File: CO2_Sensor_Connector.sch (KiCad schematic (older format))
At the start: 8 parts, among them J1 Conn_01x07_Female, J2 Conn_01x04_Female, Q1 AO3400A, Q2 AO3401A

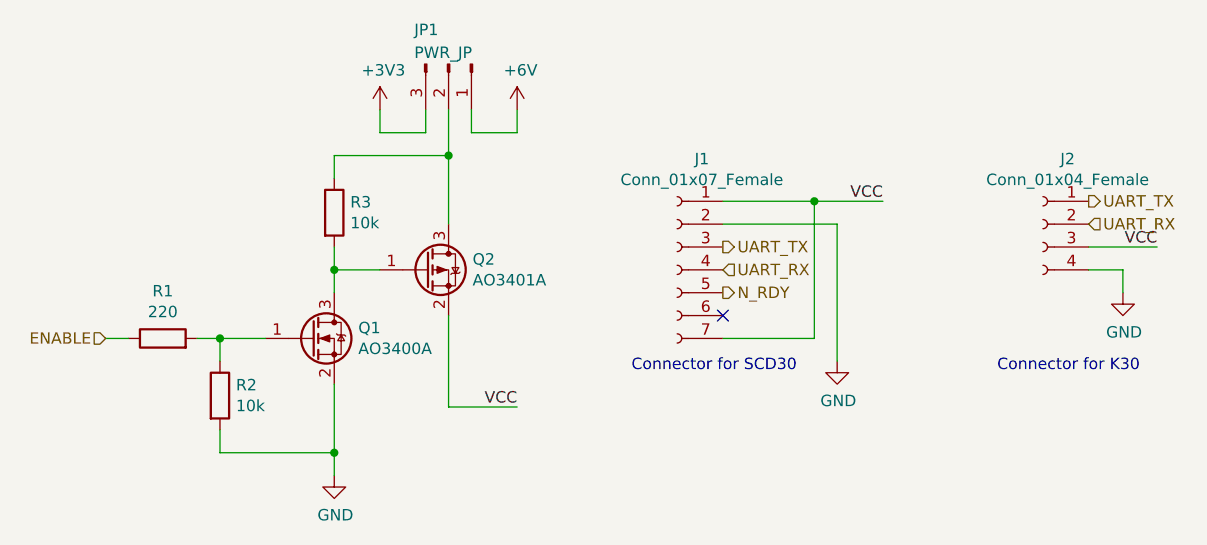
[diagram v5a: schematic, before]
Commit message: Fix sensor PMOS issue and start change to long term chamber
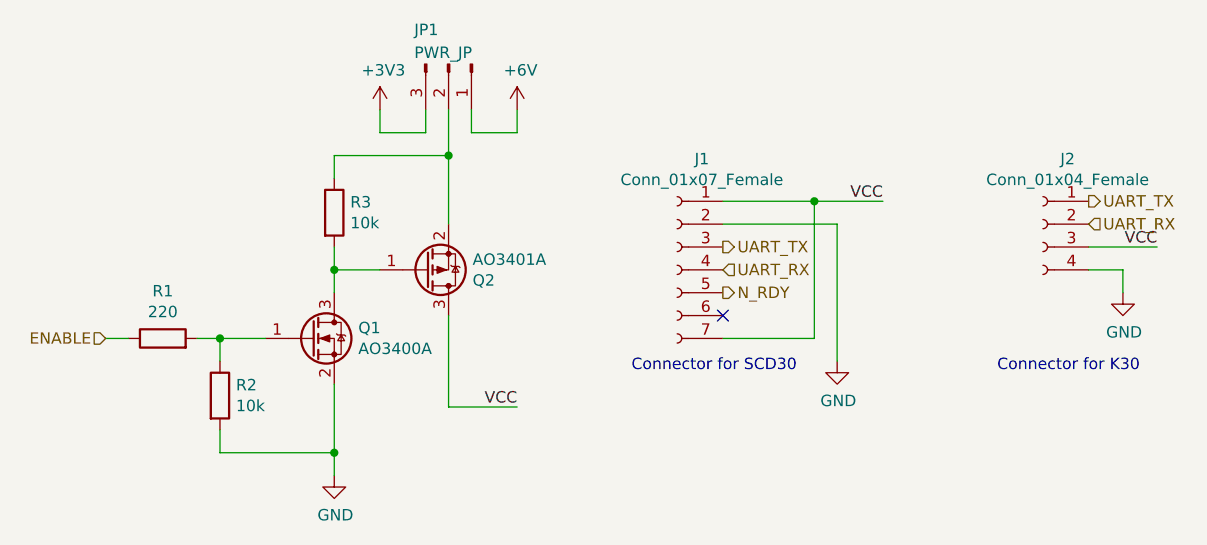
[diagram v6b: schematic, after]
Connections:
- net VCC: now also Q2.3 (D); no longer Q2.2 (S)
- net at JP1.2 (Pin_2), R3.1: now also Q2.2 (S); no longer Q2.3 (D)
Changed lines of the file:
@@
 F 4 "C15127" H 4700 3900 50  0001 C CNN "LCSC"
 	1    4700 3900
-	1    0    0    -1
+	1    0    0    1
 $EndComp
 $Comp

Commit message: Add MPPT battery charger and polyfuse, replace reverse polarity
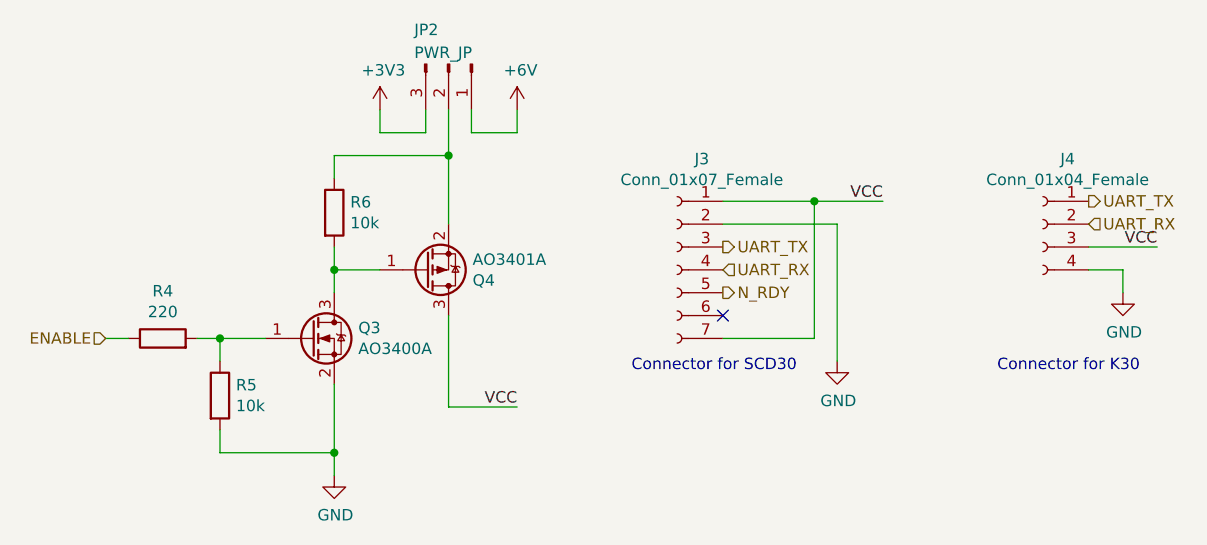
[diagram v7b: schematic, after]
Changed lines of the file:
@@
 $Descr A4 11693 8268
 encoding utf-8
-Sheet 2 9
+Sheet 3 9
 Title ""
 Date ""
@@
 AR Path="/60A49A7C/60A57B40" Ref="J1"  Part="1"
 AR Path="/60A4AC4A/60A57B40" Ref="J3"  Part="1"
-F 0 "J1" H 5692 4385 50  0000 C CNN
+F 0 "J3" H 5692 4385 50  0000 C CNN
 F 1 "Conn_01x07_Female" H 5692 4294 50  0000 C CNN
 F 2 "Connector_PinSocket_2.54mm:PinSocket_1x07_P2.54mm_Vertical" H 5800 3900 50  0001 C CNN
@@
 AR Path="/60A49A7C/60A5D6A7" Ref="#PWR04"  Part="1"
 AR Path="/60A4AC4A/60A5D6A7" Ref="#PWR09"  Part="1"
-F 0 "#PWR04" H 6500 4050 50  0001 C CNN
+F 0 "#PWR09" H 6500 4050 50  0001 C CNN
 F 1 "GND" H 6505 4127 50  0000 C CNN
 F 2 "" H 6500 4300 50  0001 C CNN
@@
 AR Path="/60A49A7C/60A6C14D" Ref="Q2"  Part="1"
 AR Path="/60A4AC4A/60A6C14D" Ref="Q4"  Part="1"
-F 0 "Q2" H 4905 3946 50  0000 L CNN
+F 0 "Q4" H 4905 3946 50  0000 L CNN
 F 1 "AO3401A" H 4905 3855 50  0000 L CNN
 F 2 "Package_TO_SOT_SMD:SOT-23" H 4900 3825 50  0001 L CIN
@@
 AR Path="/60A49A7C/60A6FA21" Ref="R1"  Part="1"
 AR Path="/60A4AC4A/60A6FA21" Ref="R4"  Part="1"
-F 0 "R1" V 3757 4200 50  0000 C CNN
+F 0 "R4" V 3757 4200 50  0000 C CNN
 F 1 "220" V 3666 4200 50  0000 C CNN
 F 2 "Resistor_SMD:R_0603_1608Metric" V 3480 4200 50  0001 C CNN
@@
 AR Path="/60A49A7C/60A736D3" Ref="R3"  Part="1"
 AR Path="/60A4AC4A/60A736D3" Ref="R6"  Part="1"
-F 0 "R3" H 4370 3696 50  0000 L CNN
+F 0 "R6" H 4370 3696 50  0000 L CNN
 F 1 "10k" H 4370 3605 50  0000 L CNN
 F 2 "Resistor_SMD:R_0603_1608Metric" V 4230 3650 50  0001 C CNN
@@
 AR Path="/60A49A7C/60A91C0B" Ref="JP1"  Part="1"
 AR Path="/60A4AC4A/60A91C0B" Ref="JP2"  Part="1"
-F 0 "JP1" V 4650 2850 50  0000 L CNN
+F 0 "JP2" V 4650 2850 50  0000 L CNN
 F 1 "PWR_JP" V 4750 2850 50  0000 L CNN
 F 2 "Connector_PinHeader_2.54mm:PinHeader_1x03_P2.54mm_Vertical" H 4800 3000 50  0001 C CNN
@@
 AR Path="/60A49A7C/60A94D4D" Ref="#PWR02"  Part="1"
 AR Path="/60A4AC4A/60A94D4D" Ref="#PWR07"  Part="1"
-F 0 "#PWR02" H 4500 3050 50  0001 C CNN
+F 0 "#PWR07" H 4500 3050 50  0001 C CNN
 F 1 "+3V3" H 4515 3373 50  0000 C CNN
 F 2 "" H 4500 3200 50  0001 C CNN
@@
 AR Path="/60A49A7C/60A9539A" Ref="#PWR03"  Part="1"
 AR Path="/60A4AC4A/60A9539A" Ref="#PWR08"  Part="1"
-F 0 "#PWR03" H 5100 3050 50  0001 C CNN
+F 0 "#PWR08" H 5100 3050 50  0001 C CNN
 F 1 "+6V" H 5115 3373 50  0000 C CNN
 F 2 "" H 5100 3200 50  0001 C CNN
@@
 AR Path="/60A49A7C/60A9EA13" Ref="#PWR01"  Part="1"
 AR Path="/60A4AC4A/60A9EA13" Ref="#PWR06"  Part="1"
-F 0 "#PWR01" H 4300 4550 50  0001 C CNN
+F 0 "#PWR06" H 4300 4550 50  0001 C CNN
 F 1 "GND" H 4305 4627 50  0000 C CNN
 F 2 "" H 4300 4800 50  0001 C CNN
@@
 AR Path="/60A49A7C/60AA508F" Ref="R2"  Part="1"
 AR Path="/60A4AC4A/60AA508F" Ref="R5"  Part="1"
-F 0 "R2" H 3870 4496 50  0000 L CNN
+F 0 "R5" H 3870 4496 50  0000 L CNN
 F 1 "10k" H 3870 4405 50  0000 L CNN
 F 2 "Resistor_SMD:R_0603_1608Metric" V 3730 4450 50  0001 C CNN
@@
 AR Path="/60A49A7C/60ABDE86" Ref="#PWR05"  Part="1"
 AR Path="/60A4AC4A/60ABDE86" Ref="#PWR010"  Part="1"
-F 0 "#PWR05" H 7750 3750 50  0001 C CNN
+F 0 "#PWR010" H 7750 3750 50  0001 C CNN
 F 1 "GND" H 7755 3827 50  0000 C CNN
 F 2 "" H 7750 4000 50  0001 C CNN
@@
 AR Path="/60A49A7C/60ABE2B1" Ref="J2"  Part="1"
 AR Path="/60A4AC4A/60ABE2B1" Ref="J4"  Part="1"
-F 0 "J2" H 7292 3985 50  0000 C CNN
+F 0 "J4" H 7292 3985 50  0000 C CNN
 F 1 "Conn_01x04_Female" H 7292 3894 50  0000 C CNN
 F 2 "Connector_PinSocket_2.54mm:PinSocket_1x04_P2.54mm_Vertical" H 7400 3700 50  0001 C CNN
@@
 AR Path="/60A49A7C/60B57C20" Ref="Q1"  Part="1"
 AR Path="/60A4AC4A/60B57C20" Ref="Q3"  Part="1"
-F 0 "Q1" H 4405 4246 50  0000 L CNN
+F 0 "Q3" H 4405 4246 50  0000 L CNN
 F 1 "AO3400A" H 4405 4155 50  0000 L CNN
 F 2 "Package_TO_SOT_SMD:SOT-23" H 4400 4125 50  0001 L CIN

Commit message: Remove all references to 6V supply which has been removed
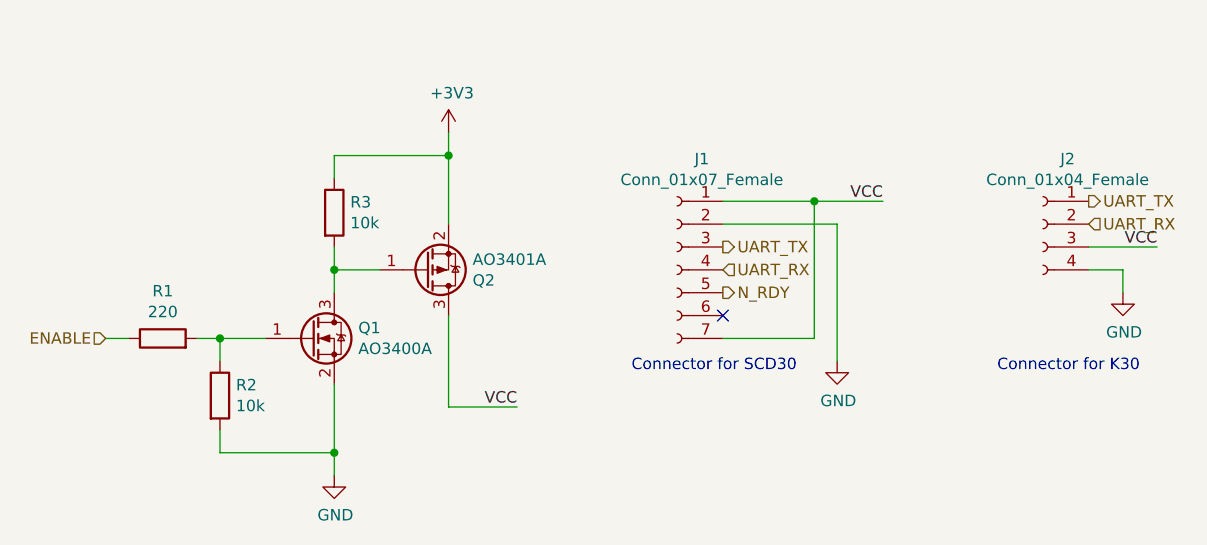
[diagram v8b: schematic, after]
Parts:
- removed JP1: PWR_JP, Connector_PinHeader_2.54mm:PinHeader_1x03_P2.54mm_Vertical, symbol Connector:Conn_01x03_Male
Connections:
- net +3V3: now also Q2.2 (S), R3.1
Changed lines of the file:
@@
 $Descr A4 11693 8268
 encoding utf-8
-Sheet 3 9
+Sheet 2 9
 Title ""
 Date ""
@@
 AR Path="/60A49A7C/60A57B40" Ref="J1"  Part="1"
 AR Path="/60A4AC4A/60A57B40" Ref="J3"  Part="1"
-F 0 "J3" H 5692 4385 50  0000 C CNN
+F 0 "J1" H 5692 4385 50  0000 C CNN
 F 1 "Conn_01x07_Female" H 5692 4294 50  0000 C CNN
 F 2 "Connector_PinSocket_2.54mm:PinSocket_1x07_P2.54mm_Vertical" H 5800 3900 50  0001 C CNN
@@
 AR Path="/60A49A7C/60A5D6A7" Ref="#PWR04"  Part="1"
 AR Path="/60A4AC4A/60A5D6A7" Ref="#PWR09"  Part="1"
-F 0 "#PWR09" H 6500 4050 50  0001 C CNN
+F 0 "#PWR04" H 6500 4050 50  0001 C CNN
 F 1 "GND" H 6505 4127 50  0000 C CNN
 F 2 "" H 6500 4300 50  0001 C CNN
@@
 AR Path="/60A49A7C/60A6C14D" Ref="Q2"  Part="1"
 AR Path="/60A4AC4A/60A6C14D" Ref="Q4"  Part="1"
-F 0 "Q4" H 4905 3946 50  0000 L CNN
+F 0 "Q2" H 4905 3946 50  0000 L CNN
 F 1 "AO3401A" H 4905 3855 50  0000 L CNN
 F 2 "Package_TO_SOT_SMD:SOT-23" H 4900 3825 50  0001 L CIN
@@
 AR Path="/60A49A7C/60A6FA21" Ref="R1"  Part="1"
 AR Path="/60A4AC4A/60A6FA21" Ref="R4"  Part="1"
-F 0 "R4" V 3757 4200 50  0000 C CNN
+F 0 "R1" V 3757 4200 50  0000 C CNN
 F 1 "220" V 3666 4200 50  0000 C CNN
 F 2 "Resistor_SMD:R_0603_1608Metric" V 3480 4200 50  0001 C CNN
@@
 AR Path="/60A49A7C/60A736D3" Ref="R3"  Part="1"
 AR Path="/60A4AC4A/60A736D3" Ref="R6"  Part="1"
-F 0 "R6" H 4370 3696 50  0000 L CNN
+F 0 "R3" H 4370 3696 50  0000 L CNN
 F 1 "10k" H 4370 3605 50  0000 L CNN
 F 2 "Resistor_SMD:R_0603_1608Metric" V 4230 3650 50  0001 C CNN
@@
 	4300 3500 4300 3400
 $Comp
-L Connector:Conn_01x03_Male JP1
-U 1 1 60A91C0B
-P 4800 3000
-AR Path="/60A49A7C/60A91C0B" Ref="JP1"  Part="1"
-AR Path="/60A4AC4A/60A91C0B" Ref="JP2"  Part="1"
-F 0 "JP2" V 4650 2850 50  0000 L CNN
-F 1 "PWR_JP" V 4750 2850 50  0000 L CNN
-F 2 "Connector_PinHeader_2.54mm:PinHeader_1x03_P2.54mm_Vertical" H 4800 3000 50  0001 C CNN
-F 3 "~" H 4800 3000 50  0001 C CNN
-F 4 "C306138" H 4800 3000 50  0001 C CNN "LCSC"
-	1    4800 3000
-	0    1    1    0
-$EndComp
-Wire Wire Line
-	4900 3200 4900 3300
-Wire Wire Line
-	4700 3200 4700 3300
-$Comp
 L power:+3V3 #PWR02
 U 1 1 60A94D4D
-P 4500 3200
+P 4800 3300
 AR Path="/60A49A7C/60A94D4D" Ref="#PWR02"  Part="1"
 AR Path="/60A4AC4A/60A94D4D" Ref="#PWR07"  Part="1"
-F 0 "#PWR07" H 4500 3050 50  0001 C CNN
-F 1 "+3V3" H 4515 3373 50  0000 C CNN
-F 2 "" H 4500 3200 50  0001 C CNN
-F 3 "" H 4500 3200 50  0001 C CNN
-	1    4500 3200
-	1    0    0    -1
-$EndComp
-$Comp
-L power:+6V #PWR03
-U 1 1 60A9539A
-P 5100 3200
-AR Path="/60A49A7C/60A9539A" Ref="#PWR03"  Part="1"
-AR Path="/60A4AC4A/60A9539A" Ref="#PWR08"  Part="1"
-F 0 "#PWR08" H 5100 3050 50  0001 C CNN
-F 1 "+6V" H 5115 3373 50  0000 C CNN
-F 2 "" H 5100 3200 50  0001 C CNN
-F 3 "" H 5100 3200 50  0001 C CNN
-	1    5100 3200
-	1    0    0    -1
-$EndComp
-Wire Wire Line
-	4500 3300 4500 3200
-Wire Wire Line
-	4500 3300 4700 3300
-Wire Wire Line
-	5100 3300 5100 3200
-Wire Wire Line
-	4900 3300 5100 3300
+F 0 "#PWR02" H 4800 3150 50  0001 C CNN
+F 1 "+3V3" H 4815 3473 50  0000 C CNN
+F 2 "" H 4800 3300 50  0001 C CNN
+F 3 "" H 4800 3300 50  0001 C CNN
+	1    4800 3300
+	1    0    0    -1
+$EndComp
+Wire Wire Line
+	4800 3400 4800 3300
 $Comp
 L power:GND #PWR01
@@
 AR Path="/60A49A7C/60A9EA13" Ref="#PWR01"  Part="1"
 AR Path="/60A4AC4A/60A9EA13" Ref="#PWR06"  Part="1"
-F 0 "#PWR06" H 4300 4550 50  0001 C CNN
+F 0 "#PWR01" H 4300 4550 50  0001 C CNN
 F 1 "GND" H 4305 4627 50  0000 C CNN
 F 2 "" H 4300 4800 50  0001 C CNN
@@
 AR Path="/60A49A7C/60AA508F" Ref="R2"  Part="1"
 AR Path="/60A4AC4A/60AA508F" Ref="R5"  Part="1"
-F 0 "R5" H 3870 4496 50  0000 L CNN
+F 0 "R2" H 3870 4496 50  0000 L CNN
 F 1 "10k" H 3870 4405 50  0000 L CNN
 F 2 "Resistor_SMD:R_0603_1608Metric" V 3730 4450 50  0001 C CNN
@@
 AR Path="/60A49A7C/60ABDE86" Ref="#PWR05"  Part="1"
 AR Path="/60A4AC4A/60ABDE86" Ref="#PWR010"  Part="1"
-F 0 "#PWR010" H 7750 3750 50  0001 C CNN
+F 0 "#PWR05" H 7750 3750 50  0001 C CNN
 F 1 "GND" H 7755 3827 50  0000 C CNN
 F 2 "" H 7750 4000 50  0001 C CNN
@@
 AR Path="/60A49A7C/60ABE2B1" Ref="J2"  Part="1"
 AR Path="/60A4AC4A/60ABE2B1" Ref="J4"  Part="1"
-F 0 "J4" H 7292 3985 50  0000 C CNN
+F 0 "J2" H 7292 3985 50  0000 C CNN
 F 1 "Conn_01x04_Female" H 7292 3894 50  0000 C CNN
 F 2 "Connector_PinSocket_2.54mm:PinSocket_1x04_P2.54mm_Vertical" H 7400 3700 50  0001 C CNN
@@
 AR Path="/60A49A7C/60B57C20" Ref="Q1"  Part="1"
 AR Path="/60A4AC4A/60B57C20" Ref="Q3"  Part="1"
-F 0 "Q3" H 4405 4246 50  0000 L CNN
+F 0 "Q1" H 4405 4246 50  0000 L CNN
 F 1 "AO3400A" H 4405 4155 50  0000 L CNN
 F 2 "Package_TO_SOT_SMD:SOT-23" H 4400 4125 50  0001 L CIN
@@
 $EndComp
 Wire Wire Line
-	4800 3200 4800 3400
-Wire Wire Line
 	4300 3400 4800 3400
-Connection ~ 4800 3400
 Wire Wire Line
 	4800 3400 4800 3700
@@
 	3800 4200 4000 4200
 NoConn ~ 6000 4100
+Connection ~ 4800 3400
 $EndSCHEMATC
